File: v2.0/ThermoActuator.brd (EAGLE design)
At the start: 99.1 x 80 mm, 68 parts, among them IC1 ULN2003AD, IC2 PCF8574T, U1 CD74HCT4051_D_16

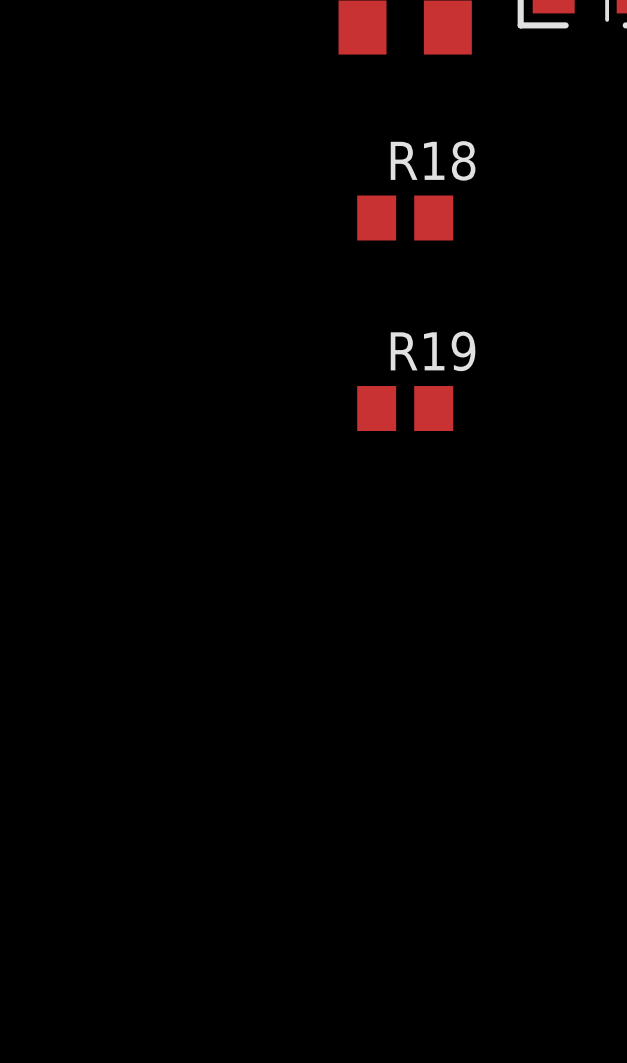
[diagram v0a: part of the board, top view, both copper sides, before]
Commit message: PCF8574 schematics ready
schematics for the I2C GPIO expander is completed
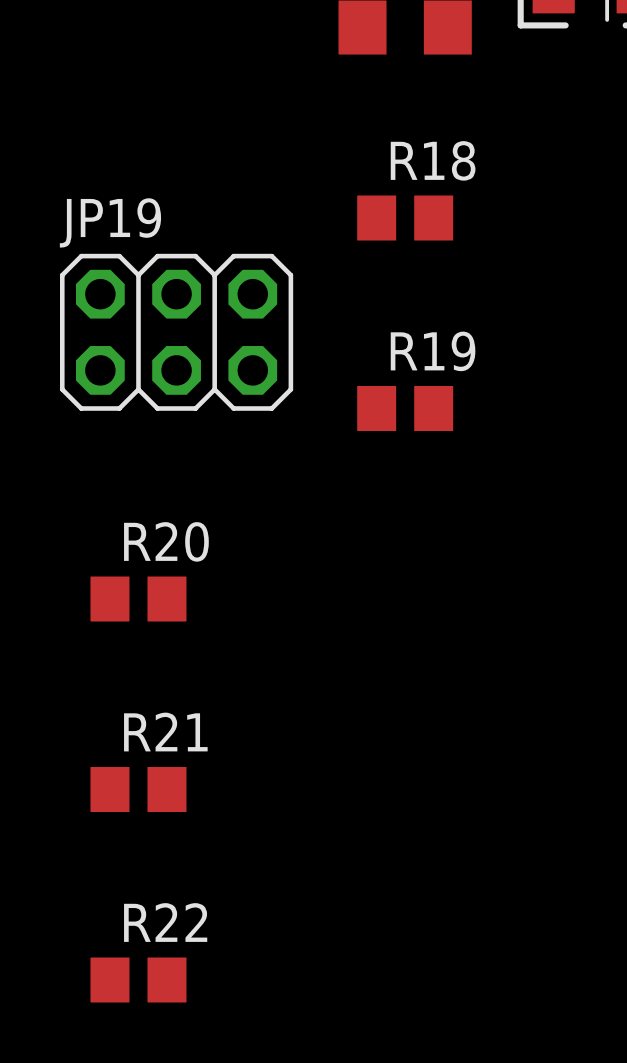
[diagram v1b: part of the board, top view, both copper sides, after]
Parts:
- added JP19: (no value), pinhead:2X03
- added R20, R21, R22: 1K, rcl:R0805
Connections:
- new net N$10: IC2.1, JP19.2, R20.1
- new net N$24: IC2.2, JP19.4, R21.1
- new net N$25: IC2.3, JP19.6, R22.1
- net GND: now also JP19.1, JP19.3, JP19.5
- net VDD: now also R20.2, R21.2, R22.2
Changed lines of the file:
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@@
 <?xml version="1.0" encoding="utf-8"?>
 <!DOCTYPE eagle SYSTEM "eagle.dtd">
-<eagle version="7.1.0">
+<eagle version="7.4.0">
 <drawing>
 <settings>
@@
 <element name="R18" library="rcl" package="R0805" value="330" x="-66.04" y="-110.49"/>
 <element name="R19" library="rcl" package="R0805" value="330" x="-66.04" y="-116.84"/>
+<element name="JP19" library="pinhead" package="2X03" value="" x="-73.66" y="-114.3"/>
+<element name="R20" library="rcl" package="R0805" value="1K" x="-74.93" y="-123.19"/>
+<element name="R21" library="rcl" package="R0805" value="1K" x="-74.93" y="-129.54"/>
+<element name="R22" library="rcl" package="R0805" value="1K" x="-74.93" y="-135.89"/>
 </elements>
 <signals>
@@
 <contactref element="U$1" pad="GND"/>
 <contactref element="IC2" pad="8"/>
+<contactref element="JP19" pad="1"/>
+<contactref element="JP19" pad="3"/>
+<contactref element="JP19" pad="5"/>
+<wire x1="-73.66" y1="-115.57" x2="-76.2" y2="-115.57" width="0" layer="19" extent="1-1"/>
+<wire x1="-71.12" y1="-115.57" x2="-73.66" y2="-115.57" width="0" layer="19" extent="1-1"/>
+<wire x1="-61.09" y1="-102.87" x2="-71.12" y2="-115.57" width="0" layer="19" extent="1-1"/>
 <wire x1="-64.77" y1="-96.52" x2="-61.09" y2="-102.87" width="0" layer="19" extent="1-1"/>
 <wire x1="-61.09" y1="-87.63" x2="-64.77" y2="-96.52" width="0" layer="19" extent="1-1"/>
@@
 <contactref element="IC2" pad="16"/>
 <contactref element="R19" pad="2"/>
+<contactref element="R22" pad="2"/>
+<contactref element="R20" pad="2"/>
 <contactref element="R18" pad="2"/>
+<contactref element="R21" pad="2"/>
+<wire x1="-73.98" y1="-129.54" x2="-73.98" y2="-135.89" width="0" layer="19" extent="1-1"/>
+<wire x1="-73.98" y1="-123.19" x2="-73.98" y2="-129.54" width="0" layer="19" extent="1-1"/>
+<wire x1="-65.09" y1="-116.84" x2="-73.98" y2="-123.19" width="0" layer="19" extent="1-1"/>
 <wire x1="-65.09" y1="-110.49" x2="-65.09" y2="-116.84" width="0" layer="19" extent="1-1"/>
 <wire x1="2.54" y1="4.76" x2="-65.09" y2="-110.49" width="0" layer="19" extent="1-1"/>
@@
 <wire x1="31.115" y1="38.89" x2="85.725" y2="14.5034" width="0" layer="19" extent="1-16"/>
 </signal>
+<signal name="N$10">
+<contactref element="JP19" pad="2"/>
+<contactref element="IC2" pad="1"/>
+<contactref element="R20" pad="1"/>
+<wire x1="-76.2" y1="-113.03" x2="-75.88" y2="-123.19" width="0" layer="19" extent="1-1"/>
+<wire x1="24.765" y1="29.69" x2="-76.2" y2="-113.03" width="0" layer="19" extent="1-1"/>
+</signal>
+<signal name="N$24">
+<contactref element="JP19" pad="4"/>
+<contactref element="IC2" pad="2"/>
+<contactref element="R21" pad="1"/>
+<wire x1="-73.66" y1="-113.03" x2="-75.88" y2="-129.54" width="0" layer="19" extent="1-1"/>
+<wire x1="26.035" y1="29.69" x2="-73.66" y2="-113.03" width="0" layer="19" extent="1-1"/>
+</signal>
+<signal name="N$25">
+<contactref element="JP19" pad="6"/>
+<contactref element="IC2" pad="3"/>
+<contactref element="R22" pad="1"/>
+<wire x1="-71.12" y1="-113.03" x2="-75.88" y2="-135.89" width="0" layer="19" extent="1-1"/>
+<wire x1="27.305" y1="29.69" x2="-71.12" y2="-113.03" width="0" layer="19" extent="1-1"/>
+</signal>
 </signals>

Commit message: 8ch mux routing complete
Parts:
- removed R11: 100K, rcl:R0805
- added JP20: (no value), pinhead:2X08
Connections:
- removed net VEE: U1.7
- new net N$26: JP20.1, JP3.1
- new net N$27: JP20.3, JP3.2
- new net N$28: JP20.5, JP3.3
- new net N$29: JP20.7, JP3.4
- new net N$30: JP20.9, JP3.5
- new net N$31: JP20.11, JP3.6
- new net N$36: JP20.10, JP20.12, JP20.14, JP20.16, JP20.2, JP20.4, JP20.6, JP20.8, U1.3
- new net N$37: JP20.13, JP3.7
- new net N$38: JP20.15, JP3.8
- net D5: now also U1.11
- net D6: now also U1.10
- net D7: now also U1.9
- net GND: now also U1.6, U1.7
- net VCC: no longer U1.16
- net VDD: now also U1.16; no longer R11.2
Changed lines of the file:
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@@
 </element>
 <element name="R2" library="rcl" package="R0805" value="330" x="85.09" y="3.683" rot="R180"/>
-<element name="R11" library="rcl" package="R0805" value="100K" x="6.35" y="60.96"/>
 <element name="R15" library="rcl" package="R1206" value="1K" x="5.08" y="54.61" rot="R270"/>
 <element name="C1" library="SparkFun-Capacitors" package="EIA3216" value="5uF" x="5.08" y="45.72" rot="R90"/>
@@
 <element name="R21" library="rcl" package="R0805" value="1K" x="-74.93" y="-129.54"/>
 <element name="R22" library="rcl" package="R0805" value="1K" x="-74.93" y="-135.89"/>
+<element name="JP20" library="pinhead" package="2X08" value="" x="-67.31" y="-144.78"/>
 </elements>
 <signals>
@@
 <contactref element="JP19" pad="3"/>
 <contactref element="JP19" pad="5"/>
+<contactref element="U1" pad="6"/>
+<contactref element="U1" pad="7"/>
 <wire x1="-73.66" y1="-115.57" x2="-76.2" y2="-115.57" width="0" layer="19" extent="1-1"/>
 <wire x1="-71.12" y1="-115.57" x2="-73.66" y2="-115.57" width="0" layer="19" extent="1-1"/>
@@
 <wire x1="5.08" y1="44.32" x2="-61.09" y2="-11.43" width="0" layer="19" extent="1-1"/>
 <wire x1="25.5778" y1="46.355" x2="5.08" y2="44.32" width="0" layer="19" extent="1-1"/>
+<wire x1="25.5778" y1="47.625" x2="25.5778" y2="46.355" width="0" layer="19" extent="1-1"/>
+<wire x1="25.5778" y1="48.895" x2="25.5778" y2="47.625" width="0" layer="19" extent="1-1"/>
+<wire x1="23.86" y1="67.183" x2="25.5778" y2="48.895" width="0" layer="19" extent="1-1"/>
+<wire x1="21.59" y1="73.66" x2="23.86" y2="67.183" width="0" layer="19" extent="1-1"/>
+<wire x1="10.16" y1="73.66" x2="21.59" y2="73.66" width="0" layer="19" extent="1-1"/>
 <wire x1="33.655" y1="29.69" x2="25.5778" y2="46.355" width="0" layer="19" extent="1-1"/>
 <wire x1="38.1" y1="18.796" x2="33.655" y2="29.69" width="0" layer="19" extent="1-1"/>
 <wire x1="40.64" y1="19.05" x2="38.1" y2="18.796" width="0" layer="19" extent="1-1"/>
-<wire x1="23.86" y1="67.183" x2="25.5778" y2="46.355" width="0" layer="19" extent="1-1"/>
-<wire x1="21.59" y1="73.66" x2="23.86" y2="67.183" width="0" layer="19" extent="1-1"/>
-<wire x1="10.16" y1="73.66" x2="21.59" y2="73.66" width="0" layer="19" extent="1-1"/>
 <wire x1="65.8" y1="45.34" x2="33.655" y2="29.69" width="0" layer="19" extent="1-1"/>
 <wire x1="91.2622" y1="24.13" x2="65.8" y2="45.34" width="0" layer="19" extent="1-1"/>
@@
 <signal name="D5">
 <contactref element="JP4" pad="6"/>
+<contactref element="U1" pad="11"/>
+<wire x1="30.3022" y1="48.895" x2="48.26" y2="67.437" width="0" layer="19" extent="1-1"/>
 </signal>
 <signal name="D6">
 <contactref element="JP4" pad="7"/>
+<contactref element="U1" pad="10"/>
+<wire x1="30.3022" y1="47.625" x2="45.72" y2="67.183" width="0" layer="19" extent="1-1"/>
 </signal>
 <signal name="D7">
 <contactref element="JP4" pad="8"/>
+<contactref element="U1" pad="9"/>
+<wire x1="30.3022" y1="46.355" x2="43.18" y2="67.437" width="0" layer="19" extent="1-1"/>
 </signal>
 <signal name="D8">
@@
 </signal>
 <signal name="VDD">
-<contactref element="R11" pad="2"/>
 <contactref element="JP15" pad="2"/>
 <contactref element="JP15" pad="1"/>
@@
 <contactref element="R18" pad="2"/>
 <contactref element="R21" pad="2"/>
+<contactref element="U1" pad="16"/>
 <wire x1="-73.98" y1="-129.54" x2="-73.98" y2="-135.89" width="0" layer="19" extent="1-1"/>
 <wire x1="-73.98" y1="-123.19" x2="-73.98" y2="-129.54" width="0" layer="19" extent="1-1"/>
@@
 <wire x1="84.14" y1="3.683" x2="86.995" y2="8.3566" width="0" layer="19" extent="1-16"/>
 <wire x1="24.765" y1="38.89" x2="21.59" y2="11.43" width="0" layer="19" extent="1-1"/>
-<wire x1="7.3" y1="60.96" x2="24.765" y2="38.89" width="0" layer="19" extent="1-1"/>
+<wire x1="30.3022" y1="55.245" x2="24.765" y2="38.89" width="0" layer="19" extent="1-1"/>
 <wire x1="91.2622" y1="67.31" x2="78.74" y2="11.43" width="0" layer="19" extent="1-1"/>
 <wire x1="94.1578" y1="67.31" x2="91.2622" y2="67.31" width="0" layer="19" extent="1-1"/>
@@
 <signal name="N$39">
 </signal>
-<signal name="VEE">
-<contactref element="U1" pad="7"/>
-</signal>
 <signal name="VCC">
-<contactref element="U1" pad="16"/>
 <contactref element="U$1" pad="VCC"/>
-<wire x1="30.3022" y1="55.245" x2="65.8" y2="61.34" width="0" layer="19" extent="1-1"/>
 </signal>
 <signal name="N$2">
@@
 <wire x1="27.305" y1="29.69" x2="-71.12" y2="-113.03" width="0" layer="19" extent="1-1"/>
 </signal>
+<signal name="N$36">
+<contactref element="JP20" pad="14"/>
+<contactref element="JP20" pad="16"/>
+<contactref element="JP20" pad="12"/>
+<contactref element="JP20" pad="10"/>
+<contactref element="U1" pad="3"/>
+<contactref element="JP20" pad="8"/>
+<contactref element="JP20" pad="6"/>
+<contactref element="JP20" pad="4"/>
+<contactref element="JP20" pad="2"/>
+<wire x1="-73.66" y1="-143.51" x2="-76.2" y2="-143.51" width="0" layer="19" extent="1-1"/>
+<wire x1="-71.12" y1="-143.51" x2="-73.66" y2="-143.51" width="0" layer="19" extent="1-1"/>
+<wire x1="-68.58" y1="-143.51" x2="-71.12" y2="-143.51" width="0" layer="19" extent="1-1"/>
+<wire x1="-66.04" y1="-143.51" x2="-68.58" y2="-143.51" width="0" layer="19" extent="1-1"/>
+<wire x1="-63.5" y1="-143.51" x2="-66.04" y2="-143.51" width="0" layer="19" extent="1-1"/>
+<wire x1="-60.96" y1="-143.51" x2="-63.5" y2="-143.51" width="0" layer="19" extent="1-1"/>
+<wire x1="-58.42" y1="-143.51" x2="-60.96" y2="-143.51" width="0" layer="19" extent="1-1"/>
+<wire x1="25.5778" y1="52.705" x2="-58.42" y2="-143.51" width="0" layer="19" extent="1-1"/>
+</signal>
+<signal name="N$26">
+<contactref element="JP3" pad="1"/>
+<contactref element="JP20" pad="1"/>
+<wire x1="48.26" y1="19.177" x2="-76.2" y2="-146.05" width="0" layer="19" extent="1-1"/>
+</signal>
+<signal name="N$27">
+<contactref element="JP20" pad="3"/>
+<contactref element="JP3" pad="2"/>
+<wire x1="50.8" y1="18.923" x2="-73.66" y2="-146.05" width="0" layer="19" extent="1-1"/>
+</signal>
+<signal name="N$28">
+<contactref element="JP20" pad="5"/>
+<contactref element="JP3" pad="3"/>
+<wire x1="53.34" y1="19.177" x2="-71.12" y2="-146.05" width="0" layer="19" extent="1-1"/>
+</signal>
+<signal name="N$29">
+<contactref element="JP20" pad="7"/>
+<contactref element="JP3" pad="4"/>
+<wire x1="55.88" y1="18.923" x2="-68.58" y2="-146.05" width="0" layer="19" extent="1-1"/>
+</signal>
+<signal name="N$30">
+<contactref element="JP20" pad="9"/>
+<contactref element="JP3" pad="5"/>
+<wire x1="58.42" y1="19.177" x2="-66.04" y2="-146.05" width="0" layer="19" extent="1-1"/>
+</signal>
+<signal name="N$31">
+<contactref element="JP20" pad="11"/>
+<contactref element="JP3" pad="6"/>
+<wire x1="60.96" y1="18.923" x2="-63.5" y2="-146.05" width="0" layer="19" extent="1-1"/>
+</signal>
+<signal name="N$37">
+<contactref element="JP20" pad="13"/>
+<contactref element="JP3" pad="7"/>
+<wire x1="63.5" y1="19.177" x2="-60.96" y2="-146.05" width="0" layer="19" extent="1-1"/>
+</signal>
+<signal name="N$38">
+<contactref element="JP20" pad="15"/>
+<contactref element="JP3" pad="8"/>
+<wire x1="66.04" y1="18.923" x2="-58.42" y2="-146.05" width="0" layer="19" extent="1-1"/>
+</signal>
 </signals>
